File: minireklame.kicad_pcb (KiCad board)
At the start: 2 copper layers, 100 x 50 mm, 134 parts, among them IC1 ATXMEGA64A4U-A, P0 CONN_01X04, P1 CONN_01X04, P10 CONN_01X04, P11 CONN_01X04, P12 CONN_01X04, P13 CONN_01X04, P14 CONN_01X04, P15 CONN_01X04, P17 Screw_Terminal_1x02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

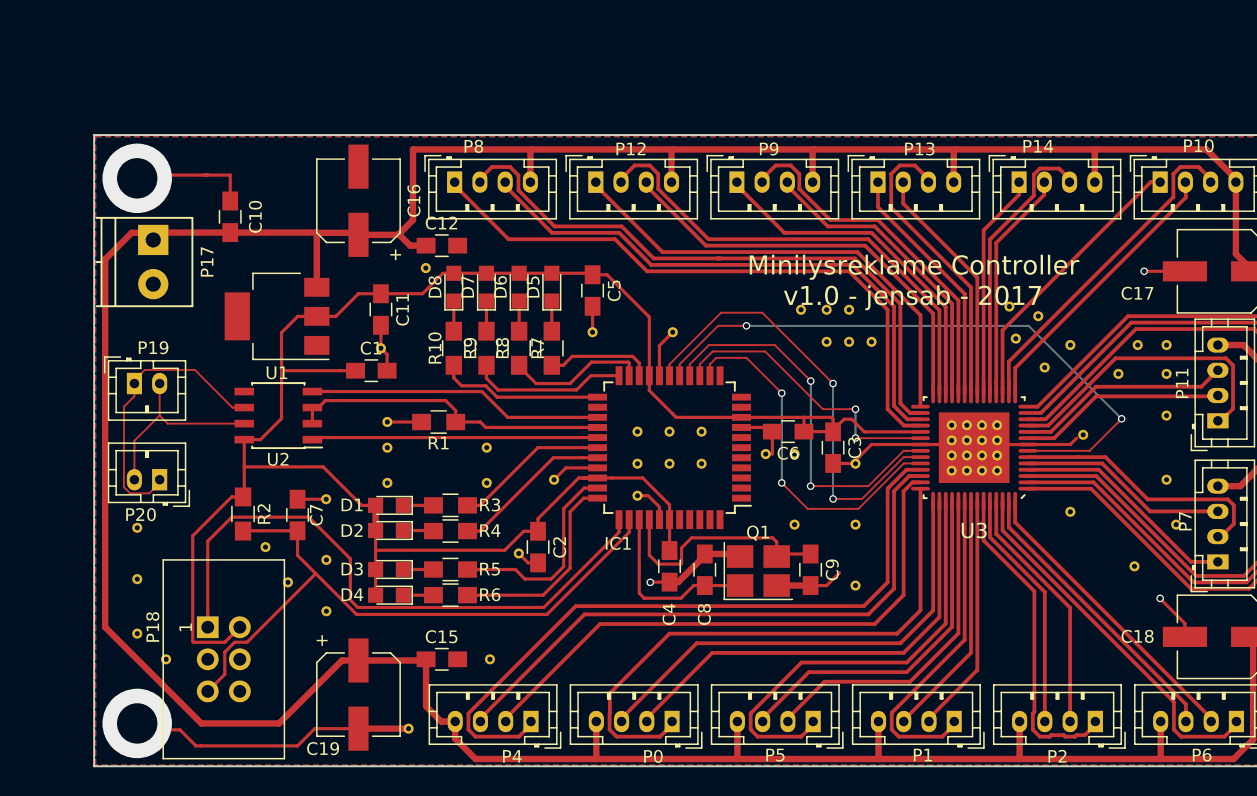
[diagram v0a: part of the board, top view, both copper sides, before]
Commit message: Updated PCB from schematic
No errors. Vias and ground plane dissappeared. Footprints and net labels should be checked against datasheets.
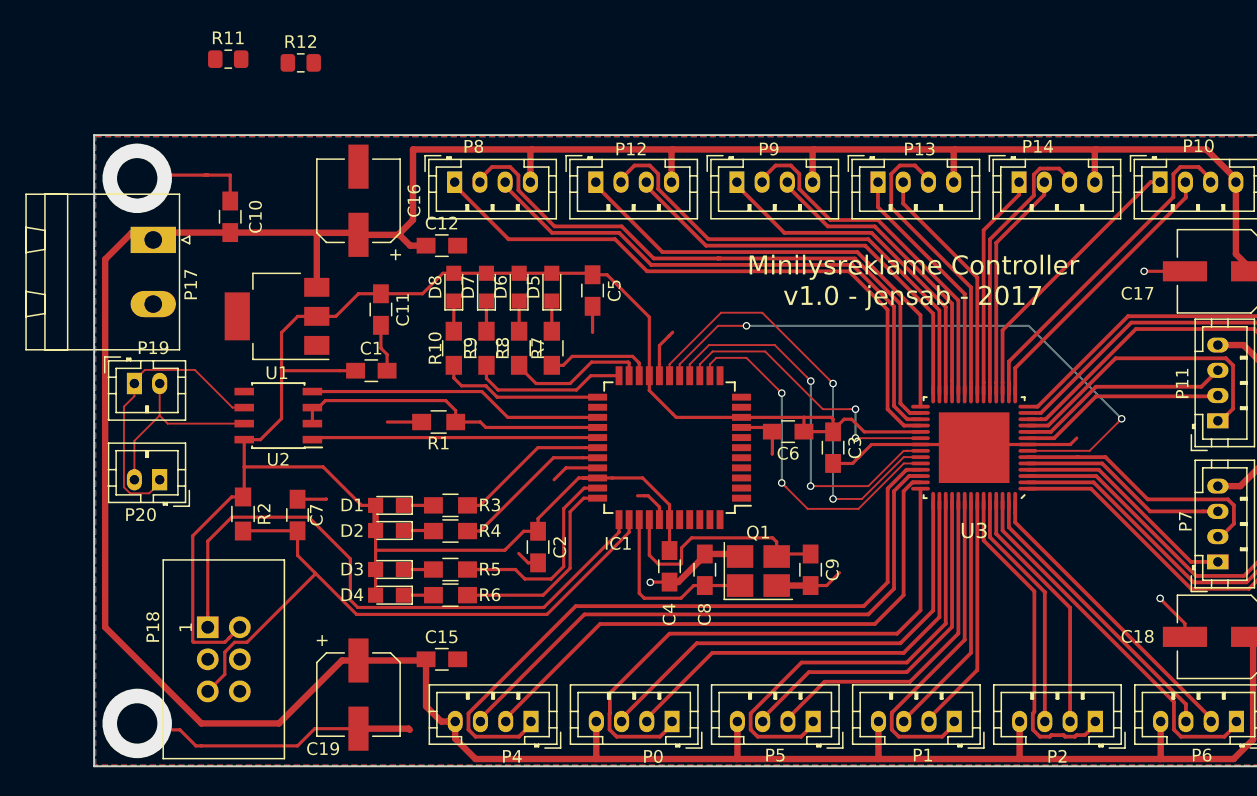
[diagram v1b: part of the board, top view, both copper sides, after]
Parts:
- removed REF** (x72): Via-0.8mm, vias:Via-0.8mm
- added R11: 10k, Resistor_SMD:R_0805_2012Metric_Pad1.15x1.40mm_HandSolder, F.Cu at (80.6, 44.0)
- added R12: 10k, Resistor_SMD:R_0805_2012Metric_Pad1.15x1.40mm_HandSolder, F.Cu at (86.4, 44.3)
- P17: value Screw_Terminal_1x02 -> Phoenix_508_2pos; footprint Connectors_Terminal_Blocks:TerminalBlock_Pheonix_PT-3.5mm_2pol -> Connector_Phoenix_MSTB:PhoenixContact_MSTBA_2,5_2-G-5,08_1x02_P5.08mm_Horizontal
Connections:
- P17 pad 1: +5V -> Net-(P17-Pad1)
- P17 pad 2: GND -> Net-(P17-Pad2)
- R1 pad 1: Net-(IC1-Pad26) -> Net-(IC1-Pad25)
- U2 pad 1: Net-(IC1-Pad27) -> Net-(IC1-Pad26)
- U2 pad 2: Net-(IC1-Pad26) -> Net-(IC1-Pad24)
- U2 pad 3: Net-(IC1-Pad26) -> Net-(IC1-Pad25)
- U2 pad 4: Net-(IC1-Pad25) -> Net-(IC1-Pad27)

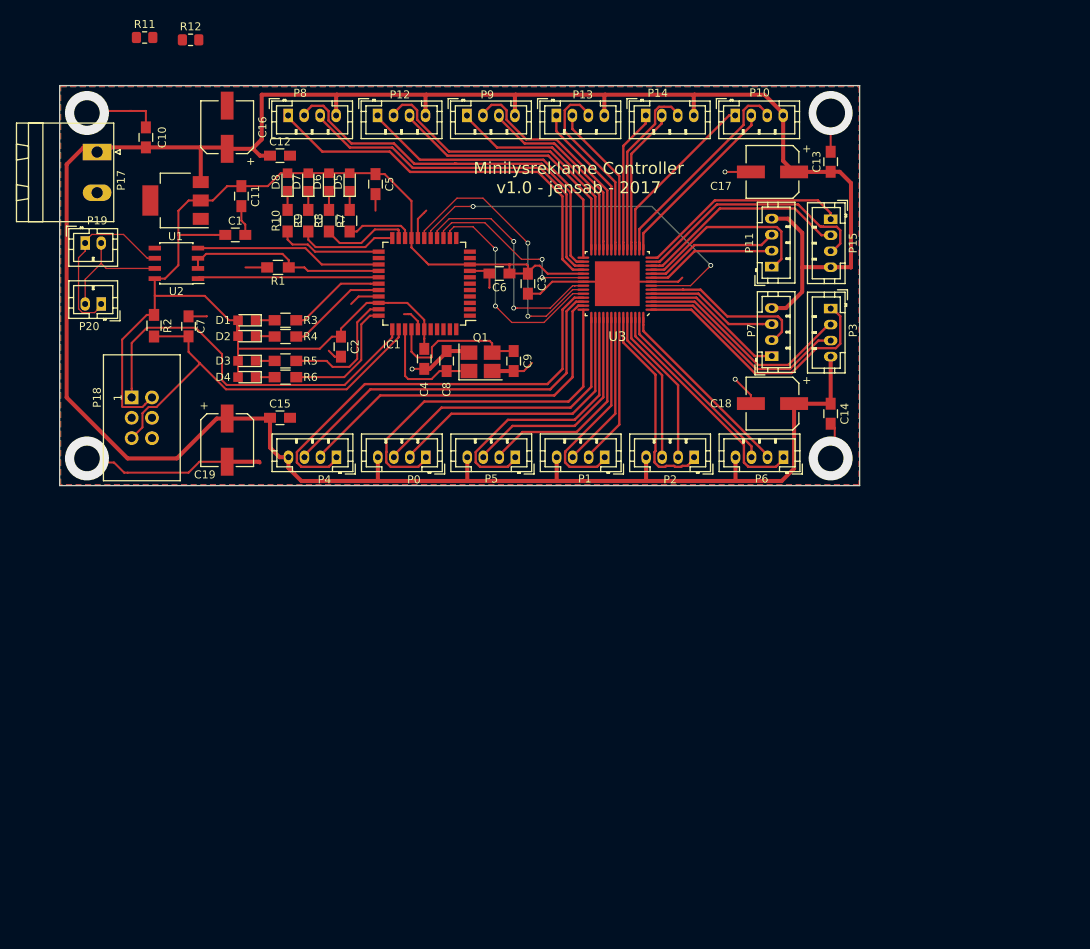
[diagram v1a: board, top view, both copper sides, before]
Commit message: New outlay
Made new PCB outlay based on the new schematic.
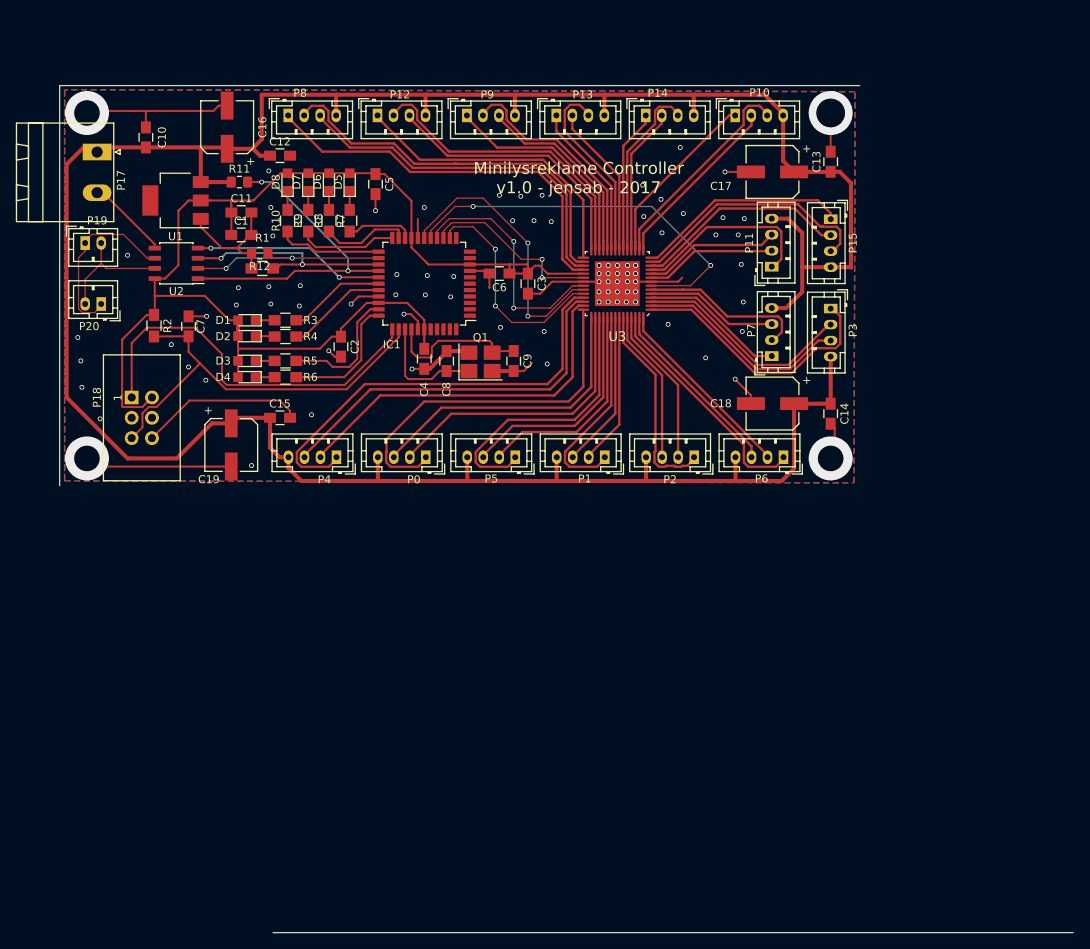
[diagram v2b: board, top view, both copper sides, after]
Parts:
- moved R12 28.0 mm to (95.0, 71.0), turned to 180 degrees
- moved R11 21.6 mm to (92.5, 62.1)
- moved C11 2.05 mm to (92.7, 65.9), turned to 0 degrees
- moved R1 1.96 mm to (95.3, 72.9)
- moved C19 0.79 mm to (91.4, 94.9)
- moved C1 0.74 mm to (92.7, 68.7)
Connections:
- P17 pad 2: Net-(P17-Pad2) -> GND
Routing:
- net GND: track 111.9 -> 156.4 mm, vias 7 -> 87
- net Net-(IC1-Pad24): track 0.00 -> 26.4 mm, vias 0 -> 2
- net Net-(IC1-Pad26): track 25.5 -> 41.3 mm, vias 0 -> 2
- net Net-(IC1-Pad25): track 24.4 -> 28.6 mm, vias 0 -> 2
- net +5V: track 332.2 -> 336.1 mm
- net +3V3: track 155.7 -> 154.2 mm
- net Net-(IC1-Pad27): track 22.7 -> 24.1 mm, vias 0 -> 2
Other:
- board size 100 x 50 mm -> 126.7 x 105.9 mm

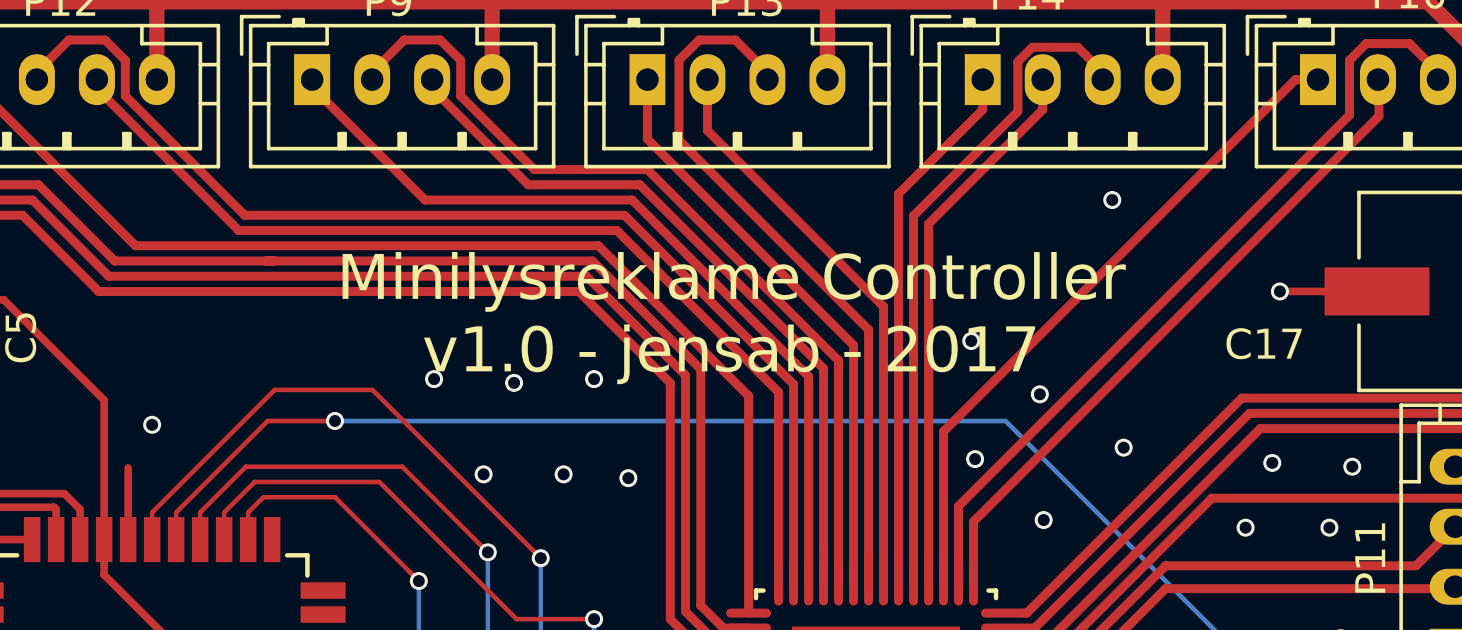
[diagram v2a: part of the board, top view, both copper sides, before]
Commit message: Updated Silkscreen
Updated silkscreen for version control.
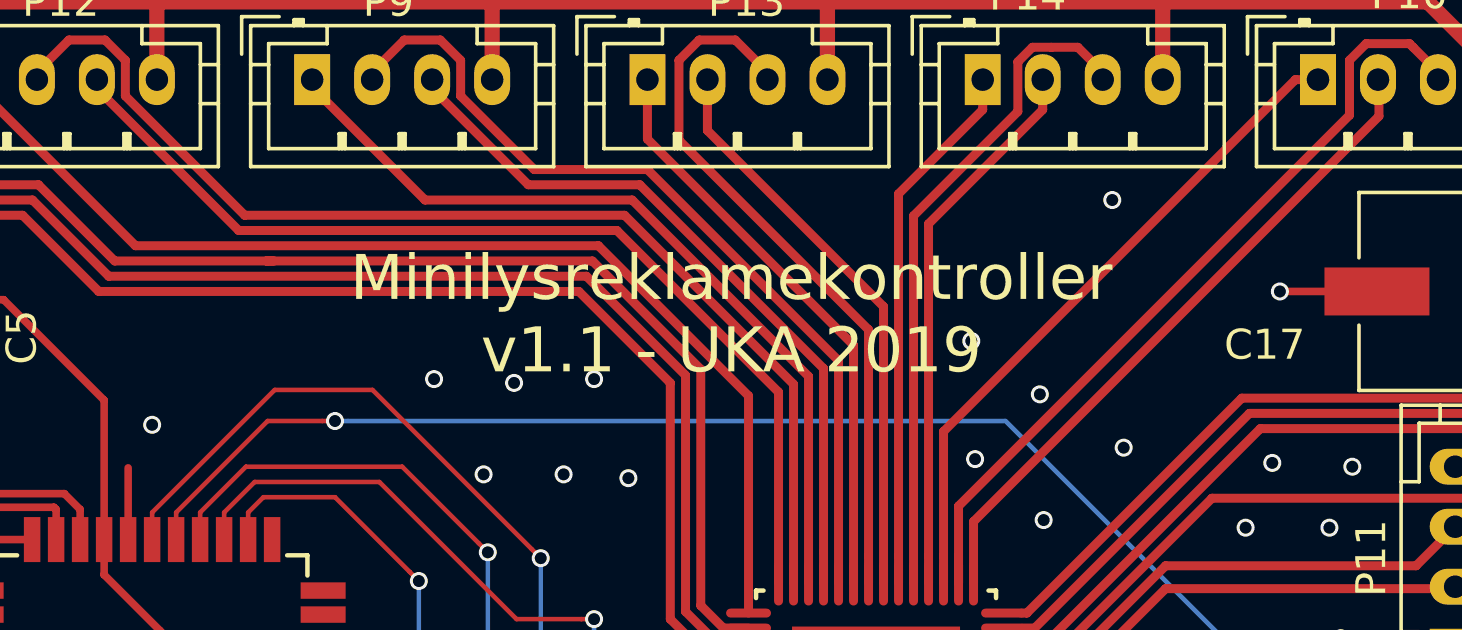
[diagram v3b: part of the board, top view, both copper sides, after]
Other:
- board text added: "Minilysreklamekontroller v1.1 - UKA 2019"
- board text removed: "Minilysreklame Controller v1.0 - jensab - 2017"
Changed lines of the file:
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@@
     )
   )
-  (gr_text "Minilysreklame Controller\nv1.0 - jensab - 2017" (at 134.879 61.552) (layer F.SilkS)
+  (gr_text "Minilysreklamekontroller\nv1.1 - UKA 2019" (at 134.879 61.552) (layer F.SilkS)
     (effects (font (size 1.5 1.5) (thickness 0.3)))
   )
@@
   (gr_line (start 196.67 155.88) (end 96.67 155.88) (layer Edge.Cuts) (width 0.15))
   (gr_line (start 70 50) (end 170 50) (layer Edge.Cuts) (width 0.15))
-  (via (at 141.991 73.49) (size 0.6) (drill 0.4) (layers F.Cu B.Cu) (net 2))
-  (via (at 140.975 73.49) (size 0.6) (drill 0.4) (layers F.Cu B.Cu) (net 2))
-  (via (at 139.705 73.49) (size 0.6) (drill 0.4) (layers F.Cu B.Cu) (net 2))
-  (via (at 138.562 73.49) (size 0.6) (drill 0.4) (layers F.Cu B.Cu) (net 2))
-  (via (at 137.419 73.49) (size 0.6) (drill 0.4) (layers F.Cu B.Cu) (net 2))
-  (via (at 141.991 75.776) (size 0.6) (drill 0.4) (layers F.Cu B.Cu) (net 2))
-  (via (at 140.975 75.776) (size 0.6) (drill 0.4) (layers F.Cu B.Cu) (net 2))
-  (via (at 139.705 75.776) (size 0.6) (drill 0.4) (layers F.Cu B.Cu) (net 2))
-  (via (at 138.562 75.776) (size 0.6) (drill 0.4) (layers F.Cu B.Cu) (net 2))
-  (via (at 137.419 75.776) (size 0.6) (drill 0.4) (layers F.Cu B.Cu) (net 2))
-  (via (at 139.705 77.046) (size 0.6) (drill 0.4) (layers F.Cu B.Cu) (net 2))
-  (via (at 138.562 77.046) (size 0.6) (drill 0.4) (layers F.Cu B.Cu) (net 2))
-  (via (at 140.848 77.046) (size 0.6) (drill 0.4) (layers F.Cu B.Cu) (net 2))
-  (via (at 141.991 77.046) (size 0.6) (drill 0.4) (layers F.Cu B.Cu) (net 2))
-  (via (at 137.419 77.046) (size 0.6) (drill 0.4) (layers F.Cu B.Cu) (net 2))
-  (via (at 139.705 72.474) (size 0.6) (drill 0.4) (layers F.Cu B.Cu) (net 2))
-  (via (at 140.975 72.474) (size 0.6) (drill 0.4) (layers F.Cu B.Cu) (net 2))
-  (via (at 138.562 72.474) (size 0.6) (drill 0.4) (layers F.Cu B.Cu) (net 2))
-  (via (at 141.991 72.474) (size 0.6) (drill 0.4) (layers F.Cu B.Cu) (net 2))
-  (via (at 137.419 72.474) (size 0.6) (drill 0.4) (layers F.Cu B.Cu) (net 2))
   (segment (start 113.975 69.06) (end 113.975 64.415) (width 0.254) (layer F.Cu) (net 1))
   (segment (start 113.975 64.415) (end 110.624 61.064) (width 0.254) (layer F.Cu) (net 1))
@@
   (segment (start 94.219 64.36) (end 91.445 64.36) (width 0.254) (layer F.Cu) (net 1))
   (segment (start 91.445 64.36) (end 88.889 64.36) (width 0.254) (layer F.Cu) (net 1))
-  (segment (start 90.937 62.566) (end 90.939 62.568) (width 0.254) (layer F.Cu) (net 6))
+  (via (at 141.991 73.49) (size 0.6) (drill 0.4) (layers F.Cu B.Cu) (net 2))
+  (via (at 140.975 73.49) (size 0.6) (drill 0.4) (layers F.Cu B.Cu) (net 2))
+  (via (at 139.705 73.49) (size 0.6) (drill 0.4) (layers F.Cu B.Cu) (net 2))
+  (via (at 138.562 73.49) (size 0.6) (drill 0.4) (layers F.Cu B.Cu) (net 2))
+  (via (at 137.419 73.49) (size 0.6) (drill 0.4) (layers F.Cu B.Cu) (net 2))
+  (via (at 141.991 75.776) (size 0.6) (drill 0.4) (layers F.Cu B.Cu) (net 2))
+  (via (at 140.975 75.776) (size 0.6) (drill 0.4) (layers F.Cu B.Cu) (net 2))
+  (via (at 139.705 75.776) (size 0.6) (drill 0.4) (layers F.Cu B.Cu) (net 2))
+  (via (at 138.562 75.776) (size 0.6) (drill 0.4) (layers F.Cu B.Cu) (net 2))
+  (via (at 137.419 75.776) (size 0.6) (drill 0.4) (layers F.Cu B.Cu) (net 2))
+  (via (at 139.705 77.046) (size 0.6) (drill 0.4) (layers F.Cu B.Cu) (net 2))
+  (via (at 138.562 77.046) (size 0.6) (drill 0.4) (layers F.Cu B.Cu) (net 2))
+  (via (at 140.848 77.046) (size 0.6) (drill 0.4) (layers F.Cu B.Cu) (net 2))
+  (via (at 141.991 77.046) (size 0.6) (drill 0.4) (layers F.Cu B.Cu) (net 2))
+  (via (at 137.419 77.046) (size 0.6) (drill 0.4) (layers F.Cu B.Cu) (net 2))
+  (via (at 139.705 72.474) (size 0.6) (drill 0.4) (layers F.Cu B.Cu) (net 2))
+  (via (at 140.975 72.474) (size 0.6) (drill 0.4) (layers F.Cu B.Cu) (net 2))
+  (via (at 138.562 72.474) (size 0.6) (drill 0.4) (layers F.Cu B.Cu) (net 2))
+  (via (at 141.991 72.474) (size 0.6) (drill 0.4) (layers F.Cu B.Cu) (net 2))
+  (via (at 137.419 72.474) (size 0.6) (drill 0.4) (layers F.Cu B.Cu) (net 2))
   (segment (start 143.955 74.51) (end 141.991 74.51) (width 0.254) (layer F.Cu) (net 2))
   (segment (start 114.775 80.46) (end 114.775 79.456) (width 0.254) (layer F.Cu) (net 2))
@@
   (segment (start 126.751 83.182) (end 124.263 83.182) (width 0.254) (layer F.Cu) (net 5))
   (segment (start 124.263 83.182) (end 124.063 83.382) (width 0.254) (layer F.Cu) (net 5))
+  (segment (start 90.937 62.566) (end 90.939 62.568) (width 0.254) (layer F.Cu) (net 6))
   (segment (start 74.701 57.722) (end 80.777 57.722) (width 0.508) (layer F.Cu) (net 6))
   (segment (start 84.643 96.604) (end 78.491 96.604) (width 0.508) (layer F.Cu) (net 6))
